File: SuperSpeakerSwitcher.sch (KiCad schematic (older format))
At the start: 57 parts, among them J1 Conn_01x02, J10 Conn_01x01, J11 Conn_01x01, J12 Conn_01x01, J13 Conn_01x01, J14 Conn_01x01, J15 Conn_01x01, J16 Conn_01x01, J17 Conn_01x01, J18 Conn_01x01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

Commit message: Bulked up the traces
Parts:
- removed J1: Conn_01x02, Connectors_Terminal_Blocks:TerminalBlock_bornier-2_P5.08mm, symbol Conn_01x02
- added J1: Conn_01x03, Connectors_Terminal_Blocks:TerminalBlock_bornier-3_P5.08mm, symbol Conn_01x03
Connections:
- net +12V: now also J1.1 (Pin_1)
- net GND: now also J1.2 (Pin_2)
- net at R1.1: now also J1.3 (Pin_3)
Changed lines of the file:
@@
 LIBS:valves
 LIBS:relay
+LIBS:SuperSpeakerSwitcher-cache
 EELAYER 25 0
 EELAYER END
@@
 $EndComp
 $Comp
-L Conn_01x02 J1
-U 1 1 5F9D9A5B
-P 7200 5000
-F 0 "J1" H 7200 5100 50  0000 C CNN
-F 1 "Conn_01x02" H 7200 4800 50  0000 C CNN
-F 2 "Connectors_Terminal_Blocks:TerminalBlock_bornier-2_P5.08mm" H 7200 5000 50  0001 C CNN
-F 3 "" H 7200 5000 50  0001 C CNN
-	1    7200 5000
-	-1   0    0    1
-$EndComp
-$Comp
 L GND #PWR01
 U 1 1 5F9D9ACD
@@
 	7700 6150 8500 6150
 Wire Wire Line
-	7400 4900 7400 4900
+	7250 4900 7400 4900
 Wire Wire Line
 	7750 4900 7700 4900
@@
 	5700 2900 5550 2900
 Wire Wire Line
-	7400 5000 7400 5000
+	7250 5000 7400 5000
 Wire Wire Line
 	1600 4700 1550 4700
@@
 Text Notes 7300 7000 0    60   ~ 0
 SUPER HEAVY DUTY SPEAKER SWITCHER\nBY DANIEL MARKS\nCREATIVE COMMONS CC-BY-SA 4.0
+$Comp
+L Conn_01x03 J1
+U 1 1 5F9E1798
+P 7050 5000
+F 0 "J1" H 7050 5200 50  0000 C CNN
+F 1 "Conn_01x03" H 7050 4800 50  0000 C CNN
+F 2 "Connectors_Terminal_Blocks:TerminalBlock_bornier-3_P5.08mm" H 7050 5000 50  0001 C CNN
+F 3 "" H 7050 5000 50  0001 C CNN
+	1    7050 5000
+	-1   0    0    1
+$EndComp
+$Comp
+L +12V #PWR?
+U 1 1 5F9E1D06
+P 7300 4800
+F 0 "#PWR?" H 7300 4650 50  0001 C CNN
+F 1 "+12V" H 7300 4940 50  0000 C CNN
+F 2 "" H 7300 4800 50  0001 C CNN
+F 3 "" H 7300 4800 50  0001 C CNN
+	1    7300 4800
+	1    0    0    -1
+$EndComp
+Wire Wire Line
+	7300 4800 7300 5100
+Wire Wire Line
+	7300 5100 7250 5100
 $EndSCHEMATC

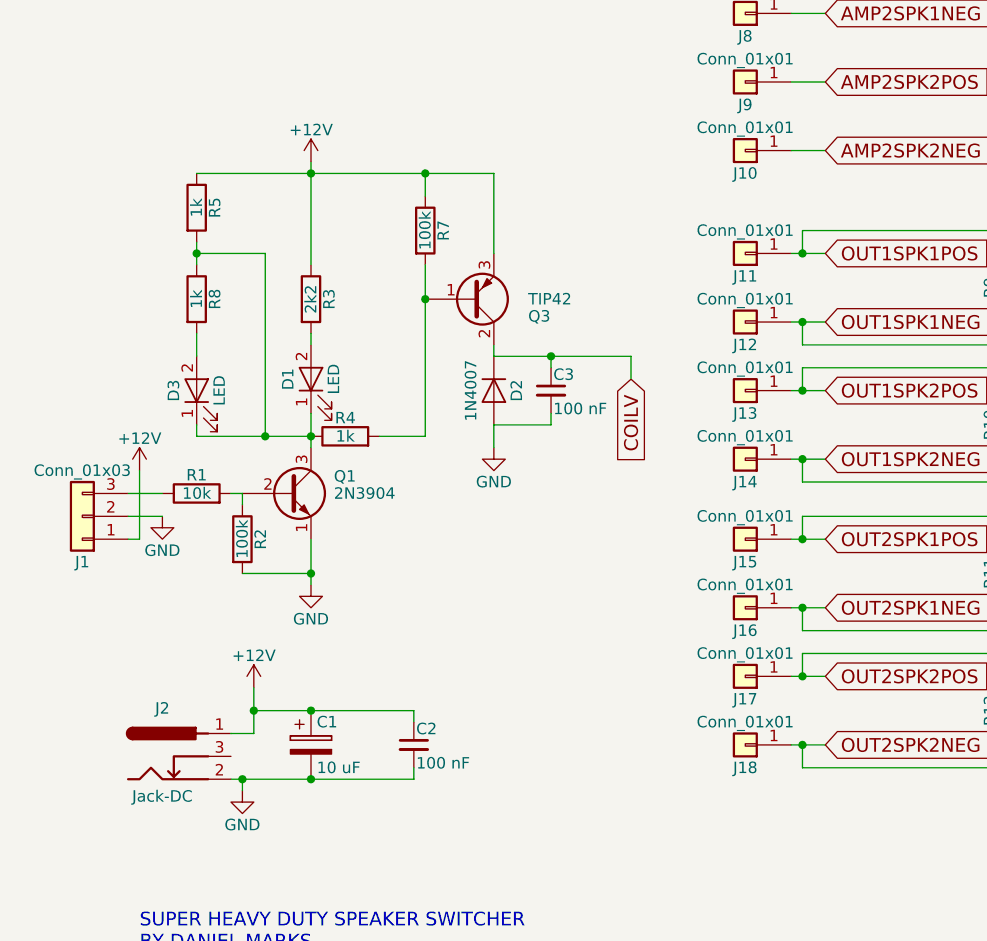
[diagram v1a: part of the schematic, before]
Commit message: Fixed on and off diodes
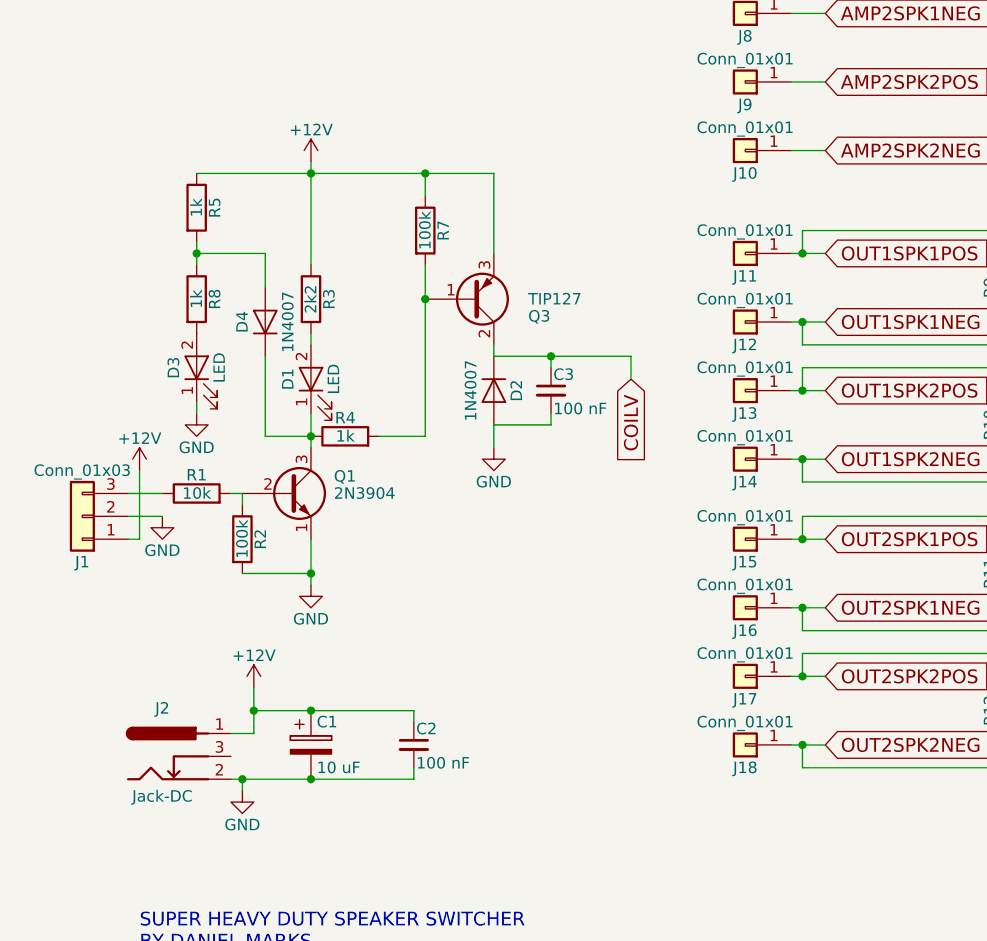
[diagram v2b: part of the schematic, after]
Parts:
- added D4: 1N4007, Diodes_THT:D_DO-41_SOD81_P7.62mm_Horizontal, symbol D
- Q3: value TIP42 -> TIP127
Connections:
- net GND: now also D3.1 (K)
- net at D1.1 (K), Q1.3 (C), R4.1: now also D4.1 (K); no longer D3.1 (K), R5.2, R8.1
- new net: D4.2 (A), R5.2, R8.1
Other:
- moved on the sheet: D3
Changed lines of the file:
@@
 $EndComp
 $Comp
-L GND #PWR01
+L GND #PWR20
 U 1 1 5F9D9ACD
 P 7750 6200
-F 0 "#PWR01" H 7750 5950 50  0001 C CNN
+F 0 "#PWR20" H 7750 5950 50  0001 C CNN
 F 1 "GND" H 7750 6050 50  0000 C CNN
 F 2 "" H 7750 6200 50  0001 C CNN
@@
 $EndComp
 $Comp
-L GND #PWR02
+L GND #PWR18
 U 1 1 5F9D9B08
 P 7400 5000
-F 0 "#PWR02" H 7400 4750 50  0001 C CNN
+F 0 "#PWR18" H 7400 4750 50  0001 C CNN
 F 1 "GND" H 7400 4850 50  0000 C CNN
 F 2 "" H 7400 5000 50  0001 C CNN
@@
 $EndComp
 $Comp
-L GND #PWR03
+L GND #PWR23
 U 1 1 5F9D9CAB
 P 8050 5300
-F 0 "#PWR03" H 8050 5050 50  0001 C CNN
+F 0 "#PWR23" H 8050 5050 50  0001 C CNN
 F 1 "GND" H 8050 5150 50  0000 C CNN
 F 2 "" H 8050 5300 50  0001 C CNN
@@
 $EndComp
 $Comp
-L +12V #PWR04
+L +12V #PWR21
 U 1 1 5F9D9CD4
 P 7800 5750
-F 0 "#PWR04" H 7800 5600 50  0001 C CNN
+F 0 "#PWR21" H 7800 5600 50  0001 C CNN
 F 1 "+12V" H 7800 5890 50  0000 C CNN
 F 2 "" H 7800 5750 50  0001 C CNN
@@
 $EndComp
 $Comp
-L GND #PWR05
+L GND #PWR24
 U 1 1 5F9D9F26
 P 8850 4700
-F 0 "#PWR05" H 8850 4450 50  0001 C CNN
+F 0 "#PWR24" H 8850 4450 50  0001 C CNN
 F 1 "GND" H 8850 4550 50  0000 C CNN
 F 2 "" H 8850 4700 50  0001 C CNN
@@
 $EndComp
 $Comp
-L +12V #PWR06
+L +12V #PWR22
 U 1 1 5F9E171B
 P 8050 3450
-F 0 "#PWR06" H 8050 3300 50  0001 C CNN
+F 0 "#PWR22" H 8050 3300 50  0001 C CNN
 F 1 "+12V" H 8050 3590 50  0000 C CNN
 F 2 "" H 8050 3450 50  0001 C CNN
@@
 L LED D3
 U 1 1 5F9E8431
-P 7550 4450
-F 0 "D3" H 7550 4550 50  0000 C CNN
-F 1 "LED" H 7550 4350 50  0000 C CNN
-F 2 "LEDs:LED_D5.0mm" H 7550 4450 50  0001 C CNN
-F 3 "" H 7550 4450 50  0001 C CNN
-	1    7550 4450
+P 7550 4350
+F 0 "D3" H 7550 4450 50  0000 C CNN
+F 1 "LED" H 7550 4250 50  0000 C CNN
+F 2 "LEDs:LED_D5.0mm" H 7550 4350 50  0001 C CNN
+F 3 "" H 7550 4350 50  0001 C CNN
+	1    7550 4350
 	0    -1   -1   0
 $EndComp
@@
 P 8750 4050
 F 0 "Q3" H 9000 4125 50  0000 L CNN
-F 1 "TIP42" H 9000 4050 50  0000 L CNN
+F 1 "TIP127" H 9000 4050 50  0000 L CNN
 F 2 "TO_SOT_Packages_THT:TO-220-3_Vertical" H 9000 3975 50  0001 L CIN
 F 3 "" H 8750 4050 50  0001 L CNN
@@
 	7750 6200 7750 6150
 Wire Wire Line
-	7700 6150 8500 6150
+	7700 6150 7750 6150
+Wire Wire Line
+	7750 6150 8050 6150
+Wire Wire Line
+	8050 6150 8500 6150
 Wire Wire Line
 	7250 4900 7400 4900
@@
 	7750 4900 7700 4900
 Wire Wire Line
-	8050 5100 8050 5300
-Wire Wire Line
-	7800 5750 7800 5950
+	8050 5100 8050 5250
+Wire Wire Line
+	8050 5250 8050 5300
+Wire Wire Line
+	7800 5750 7800 5850
+Wire Wire Line
+	7800 5850 7800 5950
 Wire Wire Line
 	7800 5950 7700 5950
@@
 Connection ~ 7750 6150
 Wire Wire Line
-	7550 4650 8050 4650
-Wire Wire Line
-	8050 4550 8050 4700
+	8050 4550 8050 4650
+Wire Wire Line
+	8050 4650 8050 4700
 Wire Wire Line
 	1600 1550 1550 1550
@@
 	10300 3400 10150 3400
 Wire Wire Line
-	10150 3850 10300 3850
-Wire Wire Line
-	10150 4150 10300 4150
-Wire Wire Line
-	10150 4450 10300 4450
-Wire Wire Line
-	10150 4750 10300 4750
-Wire Wire Line
-	10150 5100 10300 5100
-Wire Wire Line
-	10150 5400 10300 5400
-Wire Wire Line
-	10150 5700 10300 5700
-Wire Wire Line
-	10150 6000 10300 6000
+	10150 3850 10200 3850
+Wire Wire Line
+	10200 3850 10300 3850
+Wire Wire Line
+	10150 4150 10200 4150
+Wire Wire Line
+	10200 4150 10300 4150
+Wire Wire Line
+	10150 4450 10200 4450
+Wire Wire Line
+	10200 4450 10300 4450
+Wire Wire Line
+	10150 4750 10200 4750
+Wire Wire Line
+	10200 4750 10300 4750
+Wire Wire Line
+	10150 5100 10200 5100
+Wire Wire Line
+	10200 5100 10300 5100
+Wire Wire Line
+	10150 5400 10200 5400
+Wire Wire Line
+	10200 5400 10300 5400
+Wire Wire Line
+	10150 5700 10200 5700
+Wire Wire Line
+	10200 5700 10300 5700
+Wire Wire Line
+	10150 6000 10200 6000
+Wire Wire Line
+	10200 6000 10300 6000
 Wire Wire Line
 	1600 1250 1450 1250
@@
 	5700 6150 5550 6150
 Wire Wire Line
-	8050 3450 8050 3900
+	8050 3450 8050 3500
+Wire Wire Line
+	8050 3500 8050 3900
 Wire Wire Line
 	8050 4200 8050 4250
@@
 Connection ~ 8050 5250
 Wire Wire Line
-	7550 4650 7550 4600
-Wire Wire Line
-	7550 4200 7550 4300
+	7550 4550 7550 4500
+Wire Wire Line
+	7550 4200 7550 4200
 Connection ~ 8050 3500
 Wire Wire Line
-	7550 3800 7550 3900
+	7550 3800 7550 3850
+Wire Wire Line
+	7550 3850 7550 3900
 Wire Wire Line
 	7550 3850 7850 3850
-Wire Wire Line
-	7850 3850 7850 4650
-Connection ~ 7850 4650
 Connection ~ 7550 3850
 Wire Wire Line
-	7550 3500 8850 3500
+	7550 3500 8050 3500
+Wire Wire Line
+	8050 3500 8550 3500
+Wire Wire Line
+	8550 3500 8850 3500
 Wire Wire Line
 	8850 3500 8850 3850
@@
 	8550 4650 8350 4650
 Wire Wire Line
-	8550 3900 8550 4650
+	8550 3900 8550 4050
+Wire Wire Line
+	8550 4050 8550 4650
 Wire Wire Line
 	8550 3600 8550 3500
@@
 	9100 4350 9100 4300
 Wire Wire Line
-	8850 4300 9450 4300
+	8850 4300 9100 4300
+Wire Wire Line
+	9100 4300 9450 4300
 Wire Wire Line
 	9450 4300 9450 4400
@@
 	8850 4600 8850 4700
 $Comp
-L GND #PWR07
+L GND #PWR10
 U 1 1 5F9EC7A7
 P 4450 2200
-F 0 "#PWR07" H 4450 1950 50  0001 C CNN
+F 0 "#PWR10" H 4450 1950 50  0001 C CNN
 F 1 "GND" H 4450 2050 50  0000 C CNN
 F 2 "" H 4450 2200 50  0001 C CNN
@@
 $EndComp
 $Comp
-L GND #PWR08
+L GND #PWR9
 U 1 1 5F9ECA62
 P 4450 1450
-F 0 "#PWR08" H 4450 1200 50  0001 C CNN
+F 0 "#PWR9" H 4450 1200 50  0001 C CNN
 F 1 "GND" H 4450 1300 50  0000 C CNN
 F 2 "" H 4450 1450 50  0001 C CNN
@@
 $EndComp
 $Comp
-L GND #PWR09
+L GND #PWR11
 U 1 1 5F9ECD2D
 P 4450 3000
-F 0 "#PWR09" H 4450 2750 50  0001 C CNN
+F 0 "#PWR11" H 4450 2750 50  0001 C CNN
 F 1 "GND" H 4450 2850 50  0000 C CNN
 F 2 "" H 4450 3000 50  0001 C CNN
@@
 $EndComp
 $Comp
-L GND #PWR010
+L GND #PWR12
 U 1 1 5F9ECDE3
 P 4450 3750
-F 0 "#PWR010" H 4450 3500 50  0001 C CNN
+F 0 "#PWR12" H 4450 3500 50  0001 C CNN
 F 1 "GND" H 4450 3600 50  0000 C CNN
 F 2 "" H 4450 3750 50  0001 C CNN
@@
 $EndComp
 $Comp
-L GND #PWR011
+L GND #PWR4
 U 1 1 5F9ECF81
 P 1550 3750
-F 0 "#PWR011" H 1550 3500 50  0001 C CNN
+F 0 "#PWR4" H 1550 3500 50  0001 C CNN
 F 1 "GND" H 1550 3600 50  0000 C CNN
 F 2 "" H 1550 3750 50  0001 C CNN
@@
 $EndComp
 $Comp
-L GND #PWR012
+L GND #PWR3
 U 1 1 5F9ED071
 P 1550 3000
-F 0 "#PWR012" H 1550 2750 50  0001 C CNN
+F 0 "#PWR3" H 1550 2750 50  0001 C CNN
 F 1 "GND" H 1550 2850 50  0000 C CNN
 F 2 "" H 1550 3000 50  0001 C CNN
@@
 $EndComp
 $Comp
-L GND #PWR013
+L GND #PWR2
 U 1 1 5F9ED161
 P 1550 2200
-F 0 "#PWR013" H 1550 1950 50  0001 C CNN
+F 0 "#PWR2" H 1550 1950 50  0001 C CNN
 F 1 "GND" H 1550 2050 50  0000 C CNN
 F 2 "" H 1550 2200 50  0001 C CNN
@@
 $EndComp
 $Comp
-L GND #PWR014
+L GND #PWR1
 U 1 1 5F9ED2C3
 P 1550 1450
-F 0 "#PWR014" H 1550 1200 50  0001 C CNN
+F 0 "#PWR1" H 1550 1200 50  0001 C CNN
 F 1 "GND" H 1550 1300 50  0000 C CNN
 F 2 "" H 1550 1450 50  0001 C CNN
@@
 $EndComp
 $Comp
-L GND #PWR015
+L GND #PWR5
 U 1 1 5F9ED4D0
 P 1550 4700
-F 0 "#PWR015" H 1550 4450 50  0001 C CNN
+F 0 "#PWR5" H 1550 4450 50  0001 C CNN
 F 1 "GND" H 1550 4550 50  0000 C CNN
 F 2 "" H 1550 4700 50  0001 C CNN
@@
 $EndComp
 $Comp
-L GND #PWR016
+L GND #PWR6
 U 1 1 5F9ED632
 P 1550 5450
-F 0 "#PWR016" H 1550 5200 50  0001 C CNN
+F 0 "#PWR6" H 1550 5200 50  0001 C CNN
 F 1 "GND" H 1550 5300 50  0000 C CNN
 F 2 "" H 1550 5450 50  0001 C CNN
@@
 $EndComp
 $Comp
-L GND #PWR017
+L GND #PWR16
 U 1 1 5F9ED6E8
 P 4450 7000
-F 0 "#PWR017" H 4450 6750 50  0001 C CNN
+F 0 "#PWR16" H 4450 6750 50  0001 C CNN
 F 1 "GND" H 4450 6850 50  0000 C CNN
 F 2 "" H 4450 7000 50  0001 C CNN
@@
 $EndComp
 $Comp
-L GND #PWR018
+L GND #PWR7
 U 1 1 5F9ED8BC
 P 1550 6250
-F 0 "#PWR018" H 1550 6000 50  0001 C CNN
+F 0 "#PWR7" H 1550 6000 50  0001 C CNN
 F 1 "GND" H 1550 6100 50  0000 C CNN
 F 2 "" H 1550 6250 50  0001 C CNN
@@
 $EndComp
 $Comp
-L GND #PWR019
+L GND #PWR8
 U 1 1 5F9ED9AC
 P 1550 7000
-F 0 "#PWR019" H 1550 6750 50  0001 C CNN
+F 0 "#PWR8" H 1550 6750 50  0001 C CNN
 F 1 "GND" H 1550 6850 50  0000 C CNN
 F 2 "" H 1550 7000 50  0001 C CNN
@@
 $EndComp
 $Comp
-L GND #PWR020
+L GND #PWR15
 U 1 1 5F9EDCB2
 P 4450 6250
-F 0 "#PWR020" H 4450 6000 50  0001 C CNN
+F 0 "#PWR15" H 4450 6000 50  0001 C CNN
 F 1 "GND" H 4450 6100 50  0000 C CNN
 F 2 "" H 4450 6250 50  0001 C CNN
@@
 $EndComp
 $Comp
-L GND #PWR021
+L GND #PWR14
 U 1 1 5F9EDDA2
 P 4450 5450
-F 0 "#PWR021" H 4450 5200 50  0001 C CNN
+F 0 "#PWR14" H 4450 5200 50  0001 C CNN
 F 1 "GND" H 4450 5300 50  0000 C CNN
 F 2 "" H 4450 5450 50  0001 C CNN
@@
 $EndComp
 $Comp
-L GND #PWR022
+L GND #PWR13
 U 1 1 5F9EDF04
 P 4450 4700
-F 0 "#PWR022" H 4450 4450 50  0001 C CNN
+F 0 "#PWR13" H 4450 4450 50  0001 C CNN
 F 1 "GND" H 4450 4550 50  0000 C CNN
 F 2 "" H 4450 4700 50  0001 C CNN
@@
 $EndComp
 Wire Wire Line
-	7800 5850 8500 5850
+	7800 5850 8050 5850
+Wire Wire Line
+	8050 5850 8500 5850
 Wire Wire Line
 	8500 5850 8500 5900
@@
 $EndComp
 $Comp
-L +12V #PWR?
+L +12V #PWR17
 U 1 1 5F9E1D06
 P 7300 4800
-F 0 "#PWR?" H 7300 4650 50  0001 C CNN
+F 0 "#PWR17" H 7300 4650 50  0001 C CNN
 F 1 "+12V" H 7300 4940 50  0000 C CNN
 F 2 "" H 7300 4800 50  0001 C CNN
@@
 Wire Wire Line
 	7300 5100 7250 5100
+$Comp
+L GND #PWR19
+U 1 1 5F9F3A95
+P 7550 4550
+F 0 "#PWR19" H 7550 4300 50  0001 C CNN
+F 1 "GND" H 7550 4400 50  0000 C CNN
+F 2 "" H 7550 4550 50  0001 C CNN
+F 3 "" H 7550 4550 50  0001 C CNN
+	1    7550 4550
+	1    0    0    -1
+$EndComp
+Wire Wire Line
+	7850 4650 8050 4650
+$Comp
+L D D4
+U 1 1 5FAC847F
+P 7850 4150
+F 0 "D4" H 7850 4250 50  0000 C CNN
+F 1 "1N4007" H 7850 4050 50  0000 C CNN
+F 2 "Diodes_THT:D_DO-41_SOD81_P7.62mm_Horizontal" H 7850 4150 50  0001 C CNN
+F 3 "" H 7850 4150 50  0001 C CNN
+	1    7850 4150
+	0    -1   -1   0
+$EndComp
+Wire Wire Line
+	7850 3850 7850 4000
+Wire Wire Line
+	7850 4300 7850 4650
 $EndSCHEMATC
